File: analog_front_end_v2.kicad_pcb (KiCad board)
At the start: 4 copper layers, 242 parts, among them J1 Conn_Coaxial, J3 Conn_01x01_Socket, J4 Conn_01x01_Socket, U1 ADL5531, U10 PMOD 2x6, U11 LP2985-5.0, U12 LP2985-5.0, U13 LT1363, U14 MAX 735, U15 LP2985-2.5, U16 MAX889SESA, U17 MAX6102, U18 PAT1220-C-0DB, U19 PAT1220-C-0DB, U2 ADL5531, U20 PAT1220-C-0DB, U21 PAT1220-C-0DB, U22 LP2985-3.3, U23 PMOD 2x6, U3 ADL5531, U4 PE4140B-Z, U5 ADF4360-9, U6 LTC1406, U7 THS4551, U8 LT1363, U9 PMOD 2x6

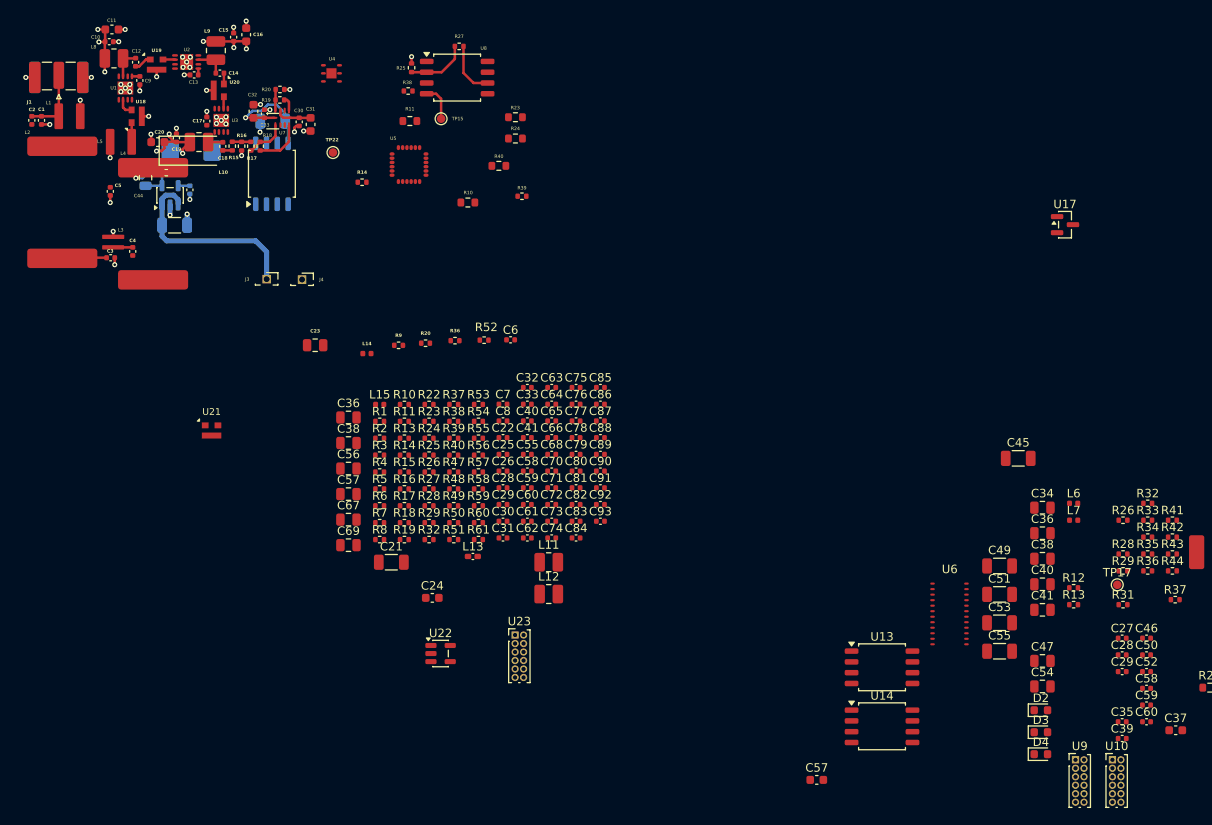
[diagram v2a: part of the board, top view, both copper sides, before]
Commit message: Remove 7 seg's from schematic/PCB, it is extra unneeded noise
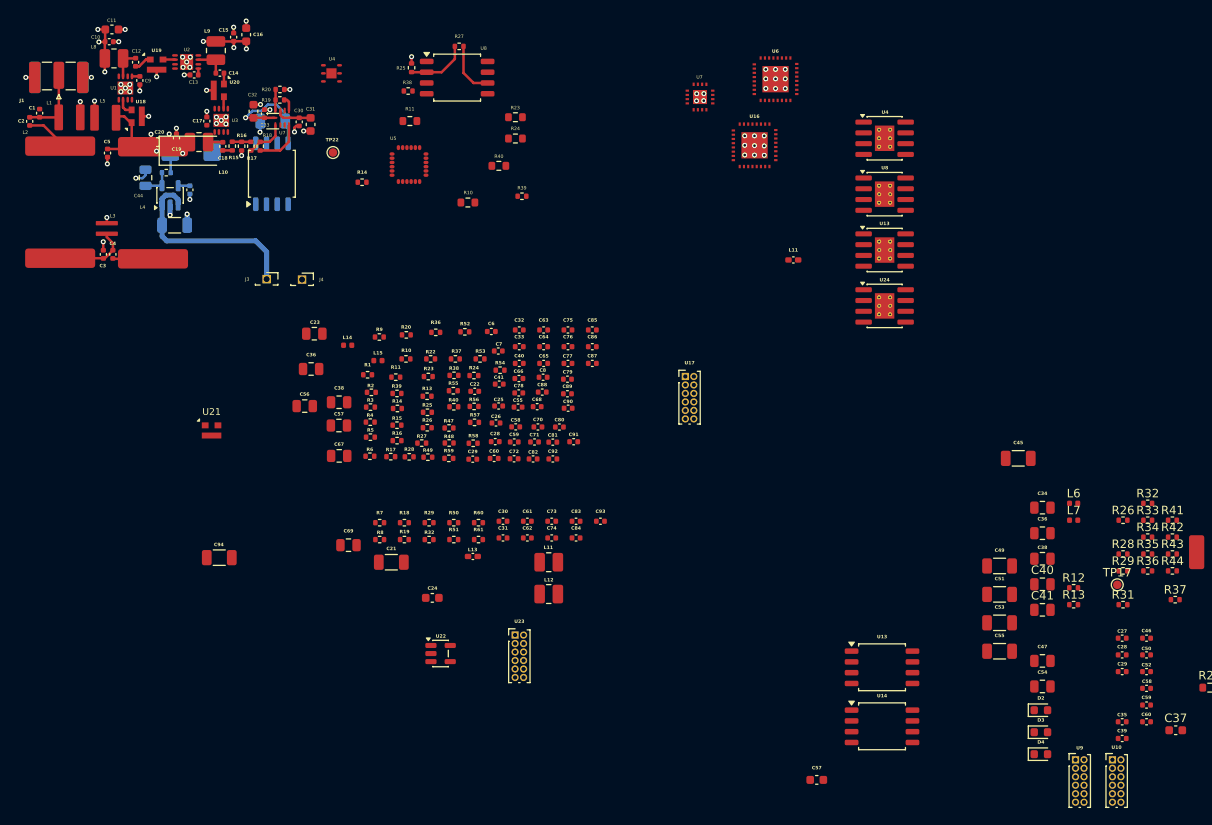
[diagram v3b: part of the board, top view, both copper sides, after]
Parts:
- removed TP15: ~, TestPoint:TestPoint_Pad_D1.0mm
- added C94: 10u_50V, Capacitor_SMD:C_1206_3216Metric, F.Cu at (36.1, 76.8)
- added L11: 160n, Inductor_SMD:L_0402_1005Metric_Pad0.77x0.64mm_HandSolder, F.Cu at (103.7, 41.8)
- added U13: ADA4899-1YRDZ, Package_SO:SOIC-8-1EP_3.9x4.9mm_P1.27mm_EP2.29x3mm_ThermalVias, F.Cu at (114.5, 40.6)
- added U16: LTC2386-16, TheEEView_Footprint_Lib:LTC2386-16, F.Cu at (99.2, 28.2)
- added U24: ADA4899-1YRDZ, Package_SO:SOIC-8-1EP_3.9x4.9mm_P1.27mm_EP2.29x3mm_ThermalVias, F.Cu at (114.5, 47.2)
- added U4: ADA4899-1YRDZ, Package_SO:SOIC-8-1EP_3.9x4.9mm_P1.27mm_EP2.29x3mm_ThermalVias, F.Cu at (114.5, 27.4)
- added U7: LT5546, TheEEView_Footprint_Lib:LT5546, F.Cu at (92.8, 22.6)
- added U8: ADA4899-1YRDZ, Package_SO:SOIC-8-1EP_3.9x4.9mm_P1.27mm_EP2.29x3mm_ThermalVias, F.Cu at (114.5, 34.0)
- R4: value 50R -> 100R
- U17: value MAX6102 -> PMOD 2x6; footprint Package_TO_SOT_SMD:SOT-23 -> Connector_PinHeader_1.00mm:PinHeader_2x06_P1.00mm_Vertical
- U6: value LTC1406 -> LTC2386-16; footprint TheEEView_Footprint_Lib:LTC1406 -> TheEEView_Footprint_Lib:LTC2386-16
- moved U6 66.3 mm to (101.7, 20.5)
- moved U17 48.2 mm to (91.0, 55.5)
- moved R24 9.09 mm to (66.1, 55.4)
- moved C56 8.99 mm to (46.2, 59.0)
- moved C79 8.92 mm to (77.1, 55.8)
- moved C88 8.71 mm to (74.2, 57.3)
- moved C78 8.57 mm to (71.4, 57.4)
- moved R39 8.53 mm to (57.0, 57.5)
- moved C90 8.33 mm to (77.2, 59.2)
- moved C57 8.16 mm to (50.2, 61.3)
- moved C89 8.13 mm to (77.1, 57.5)
- moved C66 7.97 mm to (71.4, 55.7)
- moved C92 7.76 mm to (75.4, 65.2)
- moved C67 7.59 mm to (50.2, 64.8)
- moved C82 7.38 mm to (73.1, 65.2)
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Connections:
- net 3.3V renamed 3.3V_IQ_DEMOD
- R4 pad 1: Net-(R3-Pad2) -> DEMOD_VCTRL
- R57 pad 1: ADC_I_DA+ -> ADC_I_DB+
- R57 pad 2: ADC_I_DA- -> ADC_I_DB-
- U17 pad 1: 3.3V_PMOD -> ADC_Q_DA+
- U17 pad 2: 2.5VREF -> ADC_Q_DA-
- U17 pad 3: GND -> ADC_Q_DA+
- U23 pad 1: unconnected-(U23-Pad1) -> ADC_I_DB+
- U23 pad 2: unconnected-(U23-Pad2) -> ADC_I_DB-
- U23 pad 3: unconnected-(U23-Pad3) -> ADC_Q_CNV+
- U23 pad 4: unconnected-(U23-Pad4) -> ADC_Q_CNV-
- U23 pad 7: unconnected-(U23-Pad7) -> ADC_Q_DCO+
- U23 pad 8: unconnected-(U23-Pad8) -> ADC_Q_CLK-
- U23 pad 9: unconnected-(U23-Pad9) -> ADC_Q_CLK+
- U6 pad 11: GND -> 5V_ADC
- U6 pad 13: unconnected-(U6-NC-Pad13) -> ADC_I_PDN
- U6 pad 14: unconnected-(U6-NC-Pad14) -> ADC_I_TESTPAT
- U6 pad 15: unconnected-(U6-D0-Pad15) -> ADC_I_DB-
- U6 pad 16: ADC_D1 -> ADC_I_DB+
- U6 pad 17: ADC_D2 -> ADC_I_DA-
- U6 pad 18: ADC_D3 -> ADC_I_DA+
- U6 pad 19: ADC_D4 -> ADC_I_DCO-
- U6 pad 2: 5V_ADC -> LPF_I+
- U6 pad 20: ADC_D5 -> ADC_I_DCO+
- U6 pad 21: ADC_D6 -> GND
- U6 pad 22: ADC_D7 -> 2V5_ADC
- U6 pad 23: unconnected-(U6-OFUF-Pad23) -> ADC_I_CLK-
- U6 pad 24: Net-(U6-CLK) -> ADC_I_CLK+
- U6 pad 3: 5V_ADC -> LPF_I-
- U6 pad 4: Net-(U6-VBIAS) -> GND
- U6 pad 5: 2.5VREF -> Net-(C56-Pad2)
- U6 pad 6: GND -> Net-(C56-Pad2)
- U6 pad 7: Net-(U6-AIN+) -> GND
- U6 pad 8: Net-(U6-AIN-) -> GND
- U6 pad 9: 5V_ADC -> Net-(U6-REFIN)
- U9 pad 1: unconnected-(U9-Pad1) -> ADC_I_CNV+
- U9 pad 10: ADC_D7 -> ADC_I_DCO+
- U9 pad 2: ADC_D1 -> ADC_I_CNV-
- U9 pad 3: ADC_D2 -> ADC_I_CLK+
- U9 pad 4: ADC_D3 -> ADC_I_CLK-
- U9 pad 7: ADC_D4 -> ADC_I_DA-
- U9 pad 8: ADC_D5 -> ADC_I_DA+
- U9 pad 9: ADC_D6 -> ADC_I_DCO-
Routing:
- net Net-(C5-Pad1): track 2.27 -> 9.54 mm
- net Net-(C2-Pad1): track 0.00 -> 6.89 mm
- net Net-(C4-Pad2): track 0.00 -> 4.75 mm
- net -5V_OPAMP: track 4.29 -> 0.00 mm
- net Net-(C3-Pad1): track 4.42 -> 8.66 mm
- net GND: track 30.5 -> 29.4 mm, vias 47 -> 68

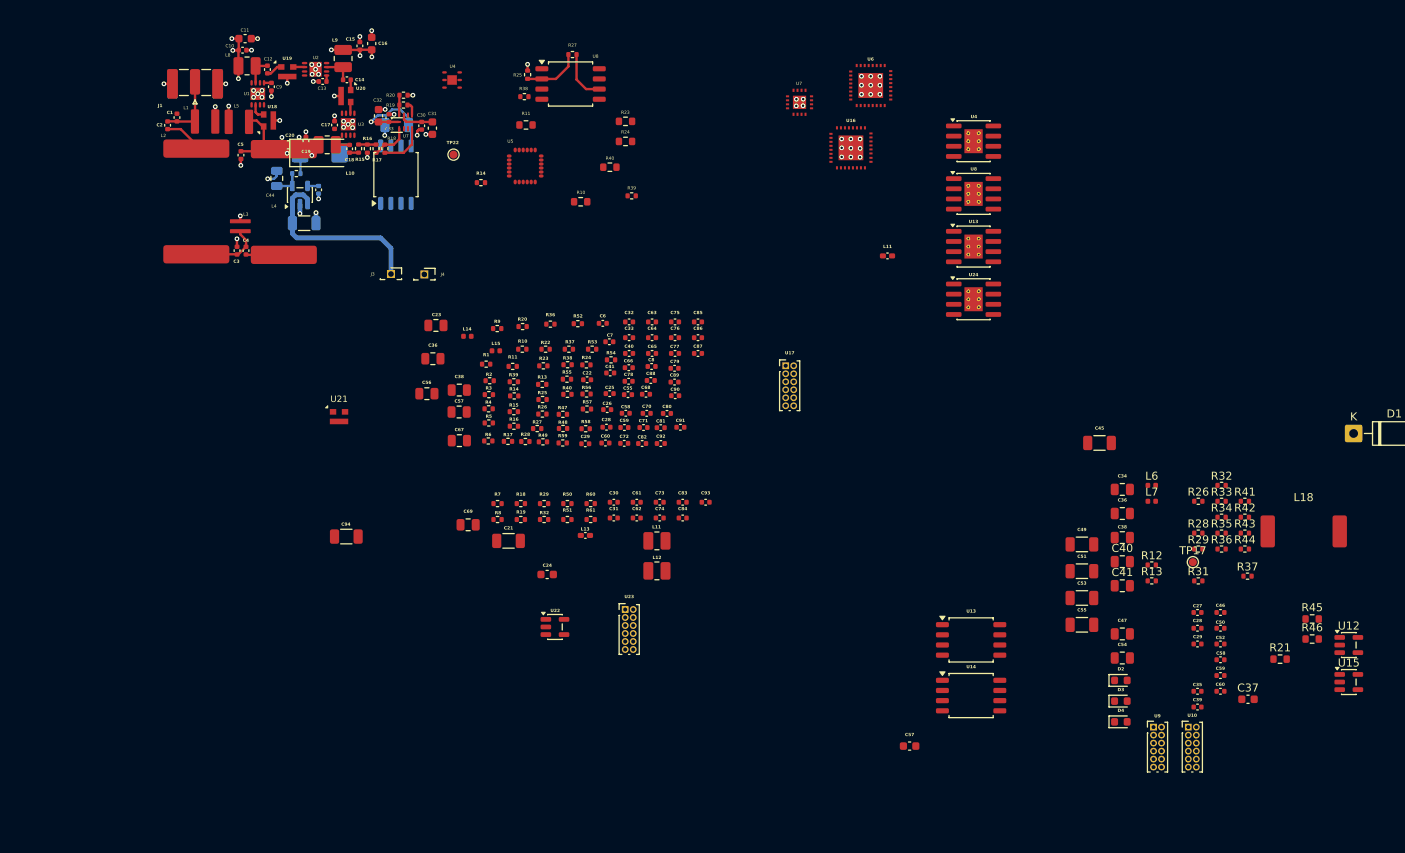
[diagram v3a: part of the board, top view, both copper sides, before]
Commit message: New RF layout attempt going horizontal
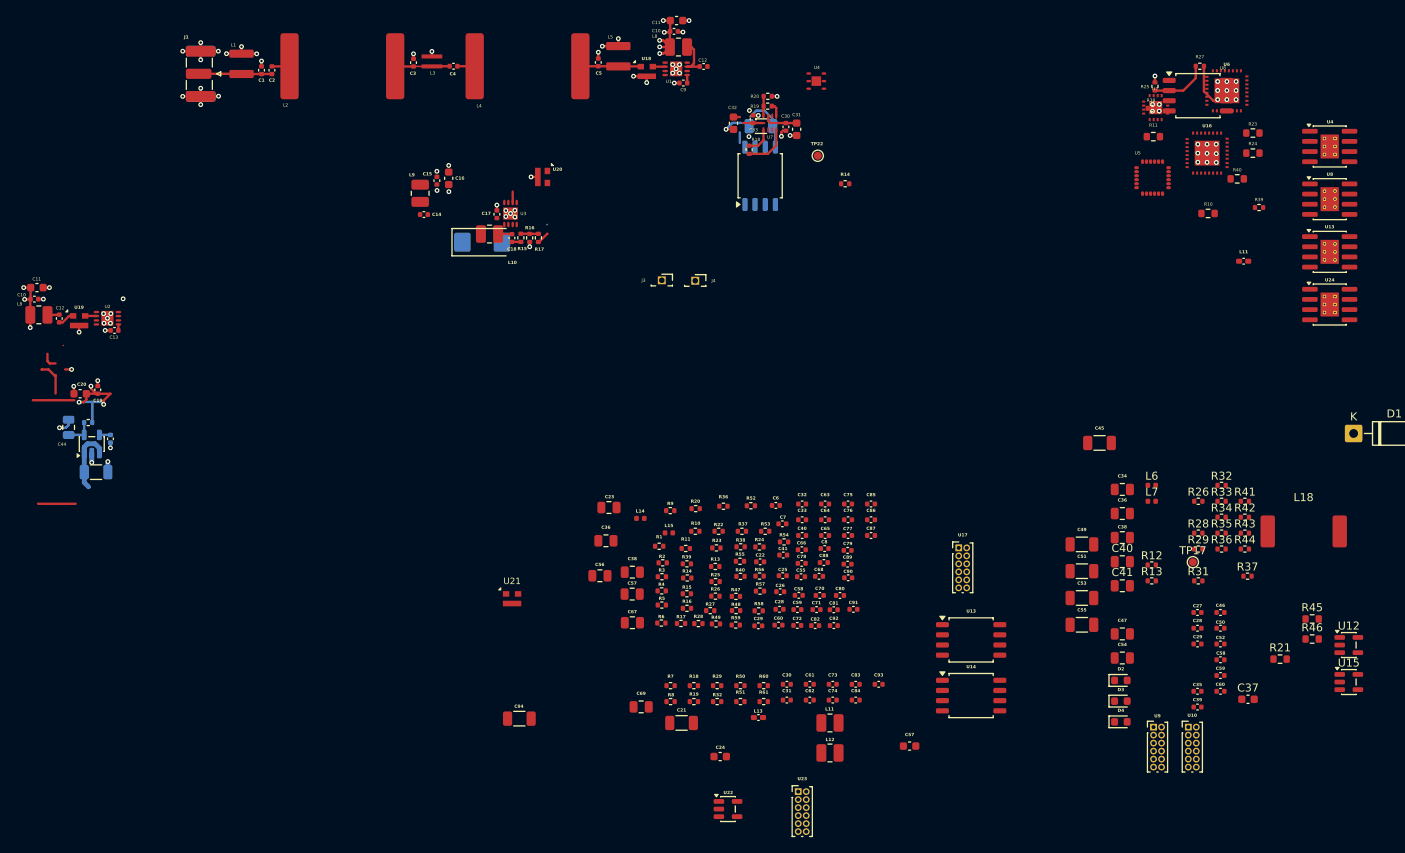
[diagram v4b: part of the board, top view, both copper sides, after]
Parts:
- added C10: 10n_25V, Capacitor_SMD:C_0402_1005Metric, F.Cu at (77.1, 13.7)
- added C11: 1u_16V, Capacitor_SMD:C_0603_1608Metric, F.Cu at (77.4, 12.3)
- added C12: 10n_25V, Capacitor_SMD:C_0402_1005Metric, F.Cu at (80.8, 18.1)
- added L8: 470n, Inductor_SMD:L_1008_2520Metric, F.Cu at (77.6, 15.7)
- moved R25 78.4 mm to (137.2, 20.6)
- moved U8 78.4 mm to (142.6, 21.7)
- moved R10 78.4 mm to (143.8, 36.5)
- moved R38 78.4 mm to (136.8, 23.3)
- moved R39 78.4 mm to (150.2, 35.7)
- moved R40 78.4 mm to (147.5, 32.1)
- moved R11 78.4 mm to (137.0, 26.9)
- moved R23 78.4 mm to (149.4, 26.4)
- moved R24 78.4 mm to (149.4, 28.9)
- moved R27 78.4 mm to (142.8, 18.1)
- moved U5 78.4 mm to (136.9, 32.0)
- moved U1 52.4 mm to (77.3, 18.4), turned to 0 degrees
- moved C9 51.5 mm to (78.2, 20.1), turned to 180 degrees
- moved L5 48.1 mm to (70.1, 16.8), turned to 90 degrees
- moved U18 47.7 mm to (73.7, 18.7), turned to 0 degrees
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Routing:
- net GND: track 29.4 -> 47.4 mm, vias 68 -> 82
- net VIN: track 23.5 -> 7.96 mm
- net Net-(C5-Pad1): track 9.54 -> 17.0 mm
- net Net-(C2-Pad1): track 6.89 -> 2.21 mm
- net Net-(U2-RFOUT): track 3.66 -> 0.01 mm
- net Net-(U1-RFOUT): track 3.60 -> 6.81 mm
- net 5V_LNA: track 27.0 -> 29.7 mm, vias 9 -> 14
- net Net-(C4-Pad2): track 4.75 -> 6.91 mm
- net Net-(C3-Pad1): track 8.66 -> 6.85 mm
- net Net-(U1-RFIN): track 2.06 -> 3.60 mm
- net Net-(C14-Pad2): track 1.28 -> 0.00 mm
- net Net-(J1-In): track 8.28 -> 8.79 mm
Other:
- board text added: "TODO: Add solid GND planes on layers 2/3 Ground via stitching Decisions: Use 0.3mm trace for 50ohm characteristic impedance for microstrip with solid groundplane in layers 2,3 oriented horizontally for EM fields Use 0.4mm silkscreen width/height to balance readability/placement Ensure RF Mixer (U4) is far away from sensitive RF/analog front end"
- board text removed: "TODO: Add solid GND planes on layers 2/3 Ground via stitching Decisions: Use 0.3mm trace for 50ohm characteristic impedance for microstrip with solid groundplane in layers 2,3 Use 0.4mm silkscreen width/height to balance readability/placement Ensure RF Mixer (U4) is far away from sensitive RF/analog front end"

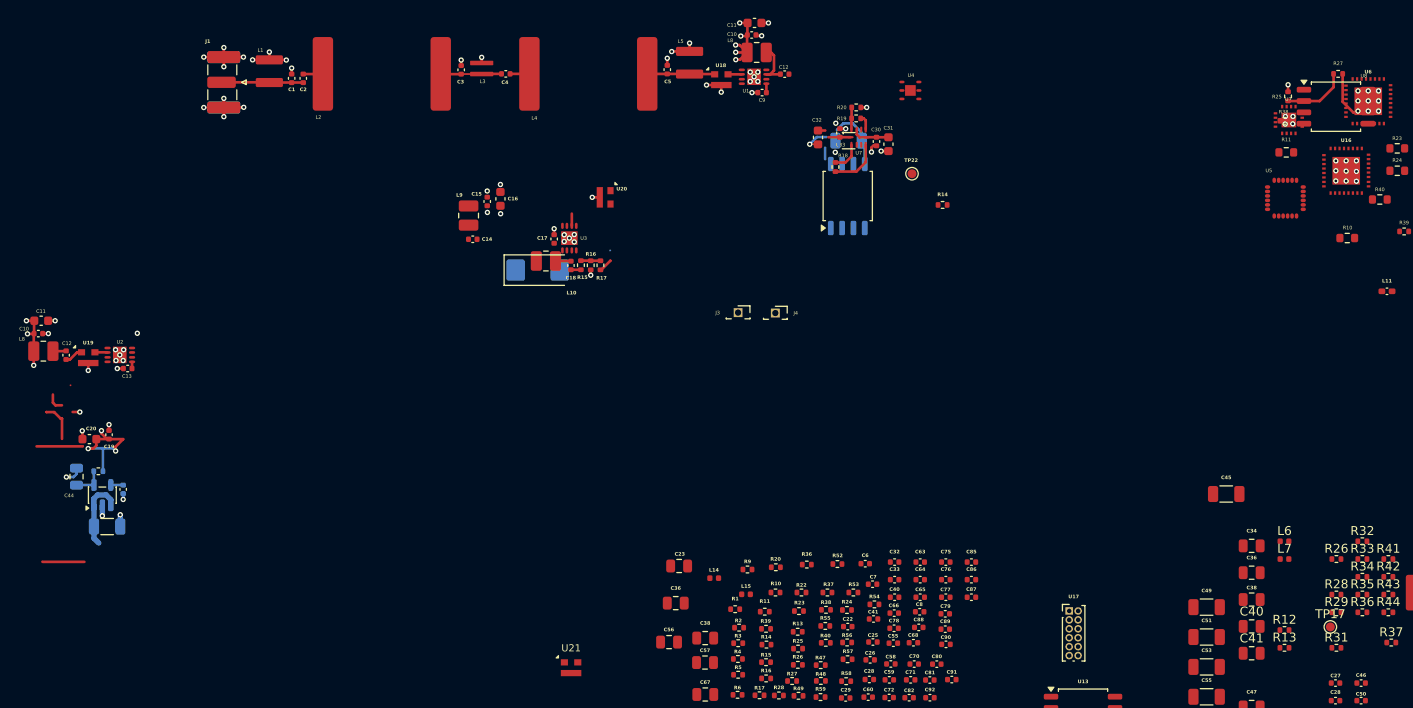
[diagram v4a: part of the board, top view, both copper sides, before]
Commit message: Add PCB notes on via stiching/guarding and implement it around the RF path
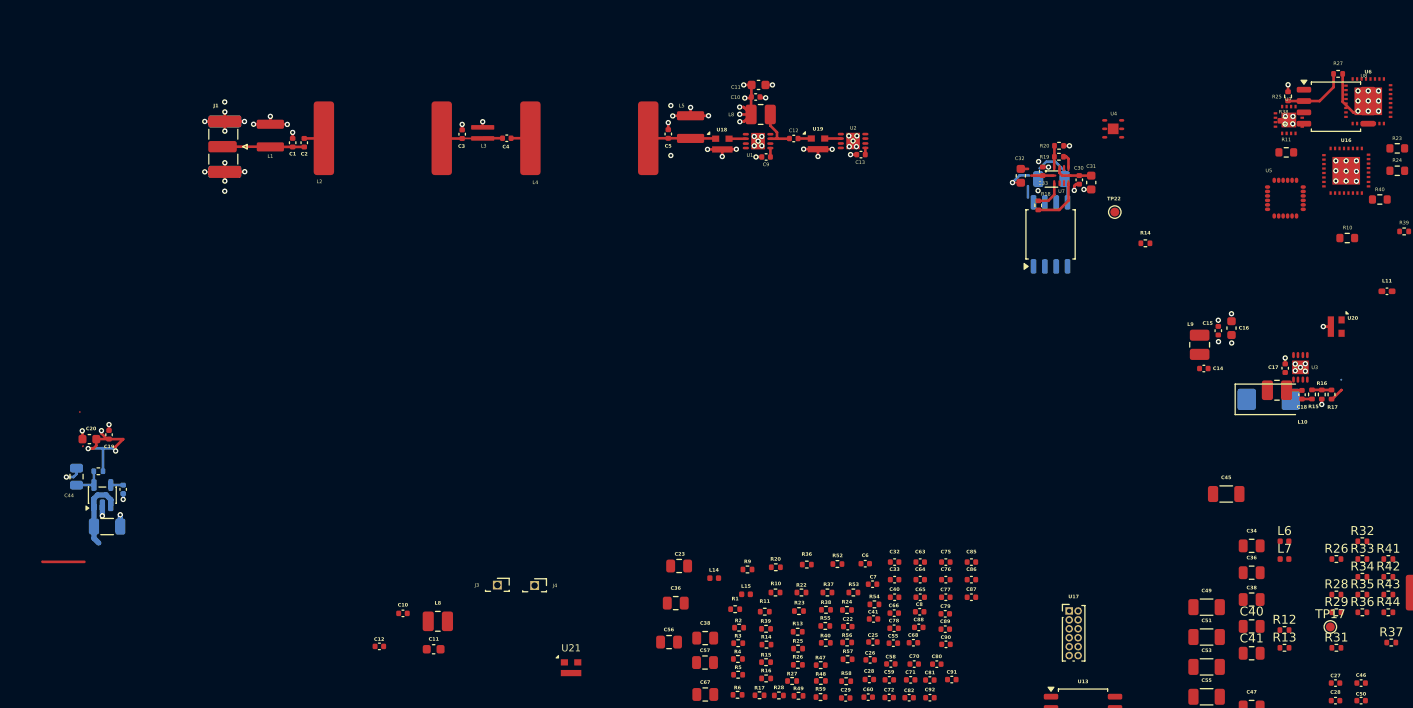
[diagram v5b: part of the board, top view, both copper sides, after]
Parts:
- moved C13 85.6 mm to (89.3, 27.1)
- moved U2 85.6 mm to (88.4, 25.6)
- moved U19 85.2 mm to (84.5, 25.9)
- moved C15 83.2 mm to (129.4, 46.8)
- moved C17 83.2 mm to (136.9, 51.0)
- moved C18 83.2 mm to (138.7, 54.0)
- moved C48 83.2 mm to (135.0, 54.5)
- moved R15 83.2 mm to (139.9, 54.0)
- moved R17 83.2 mm to (142.1, 54.0)
- moved C14 83.2 mm to (127.7, 51.1)
- moved C16 83.2 mm to (130.8, 46.5)
- moved L10 83.2 mm to (135.9, 53.5)
- moved L9 83.2 mm to (127.3, 48.4)
- moved R16 83.2 mm to (141.0, 54.0)
- moved U3 83.2 mm to (138.6, 50.9)
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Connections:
- U13 pad 9: GND -> unconnected-(U13-PAD-Pad9)
- U24 pad 9: GND -> unconnected-(U24-PAD-Pad9)
- U4 pad 9: GND -> unconnected-(U4-PAD-Pad9)
- U8 pad 9: GND -> unconnected-(U8-PAD-Pad9)
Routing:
- net Net-(C5-Pad1): track 17.0 -> 7.53 mm
- net 5V_LNA: track 29.7 -> 23.0 mm, vias 14 -> 10
- net GND: track 47.4 -> 51.9 mm, vias 82 -> 87
- net Net-(U1-RFIN): track 3.60 -> 1.54 mm
- net Net-(U1-RFOUT): track 6.81 -> 5.18 mm
- net Net-(U3-RFIN): track 1.42 -> 0.05 mm
- net Net-(C12-Pad2): track 2.06 -> 1.49 mm
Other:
- board text added: "TODO: Add solid GND planes on layers 2/3 Ground via stitching Decisions: Add ground stiching vias every lamba/10 to lambda/20 assuming er or 4.3 to 4.5 for FR4 which is 3.0 to 3.3mm for microstrip. Place vias every 3-5x trace width (1-1.2mm) Use 0.3mm trace for 50ohm characteristic impedance for microstrip with solid groundplane in layers 2,3 oriented horizontally for EM fields Use 0.4mm silkscre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"
- board text removed: "TODO: Add solid GND planes on layers 2/3 Ground via stitching Decisions: Use 0.3mm trace for 50ohm characteristic impedance for microstrip with solid groundplane in layers 2,3 oriented horizontally for EM fields Use 0.4mm silkscreen width/height to balance readability/placement Ensure RF Mixer (U4) is far away from sensitive RF/analog front end"
